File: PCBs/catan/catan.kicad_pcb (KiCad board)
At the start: 2 copper layers, 95.3 x 110 mm, 66 parts, among them J1 Conn_01x04_Female, J2 Conn_01x06_Male, SW1 SW_MEC_5E, SW10 SW_MEC_5E, SW11 SW_MEC_5E, SW2 SW_MEC_5E, SW3 SW_MEC_5E, SW4 SW_MEC_5E, SW5 SW_MEC_5E, SW6 SW_MEC_5E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

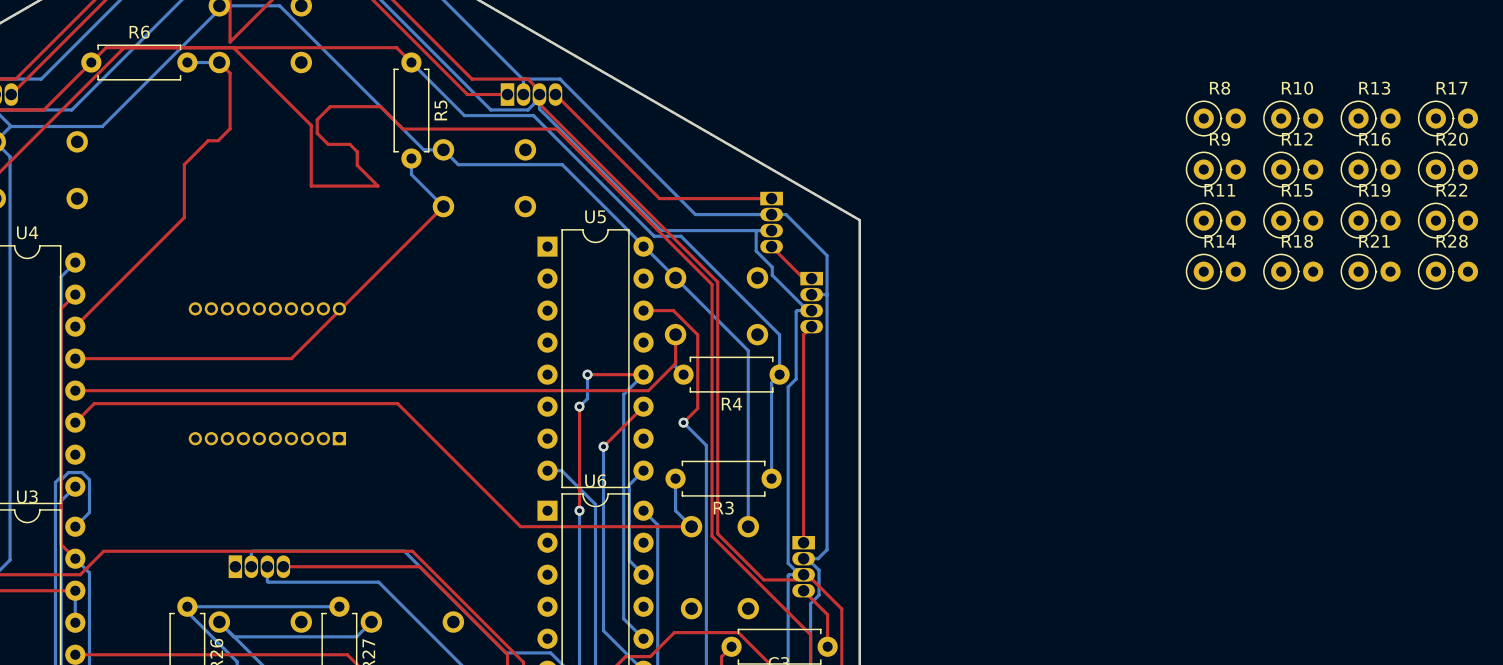
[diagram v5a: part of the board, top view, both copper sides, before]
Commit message: replace segment display
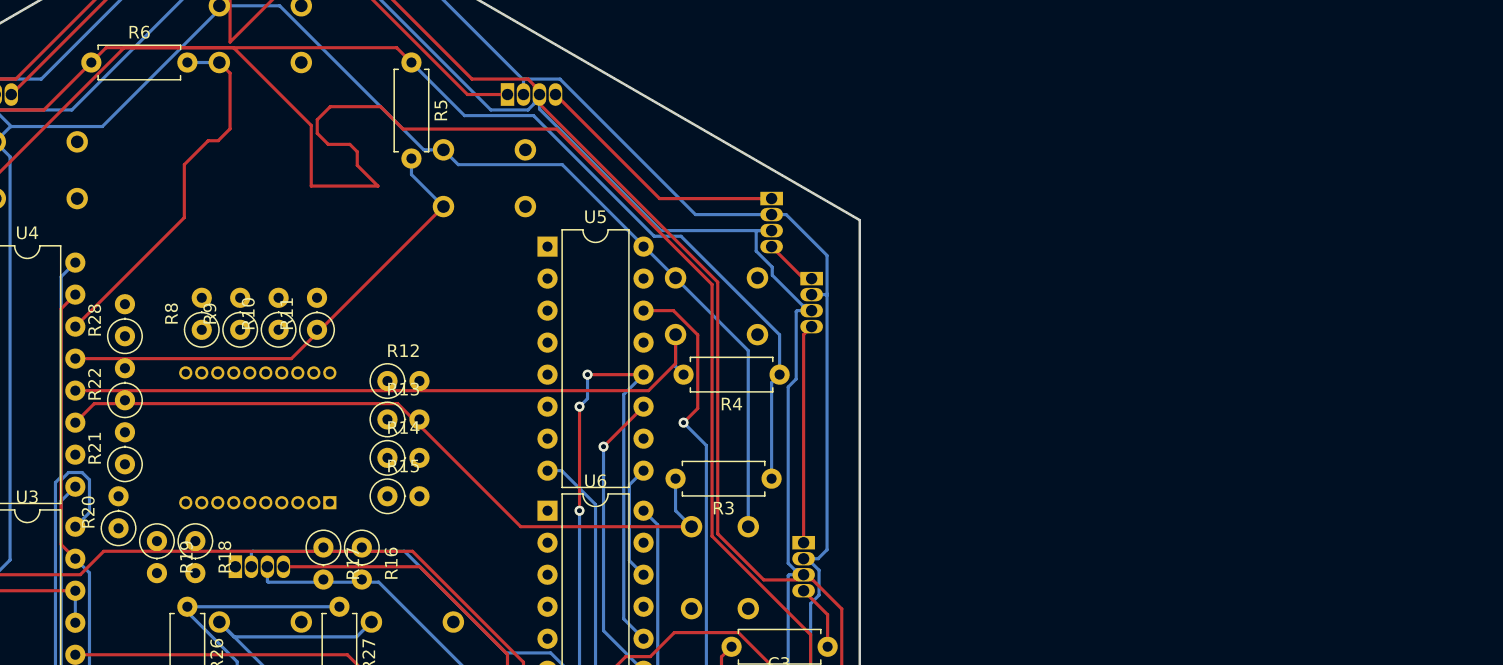
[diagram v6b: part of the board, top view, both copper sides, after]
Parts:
- moved R20 108.3 mm to (113.9, 87.1), turned to 90 degrees
- moved R22 105.0 mm to (114.4, 77.0), turned to 90 degrees
- moved R28 104.1 mm to (114.4, 71.9), turned to 90 degrees
- moved R21 99.1 mm to (114.4, 82.0), turned to 90 degrees
- moved R19 98.7 mm to (117.0, 88.1), turned to 270 degrees
- moved R17 94.6 mm to (130.2, 88.6), turned to 270 degrees
- moved R18 88.8 mm to (120.0, 88.1), turned to 270 degrees
- moved R16 84.6 mm to (133.2, 88.6), turned to 270 degrees
- moved R10 81.3 mm to (126.6, 71.4), turned to 90 degrees
- moved R8 81.3 mm to (120.5, 71.4), turned to 90 degrees
- moved R13 80.7 mm to (135.3, 78.5)
- moved R9 77.5 mm to (123.6, 71.4), turned to 90 degrees
- moved R15 74.2 mm to (135.3, 84.6)
- moved R12 72.9 mm to (135.3, 75.4)
- moved R11 70.9 mm to (129.7, 71.4), turned to 90 degrees
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
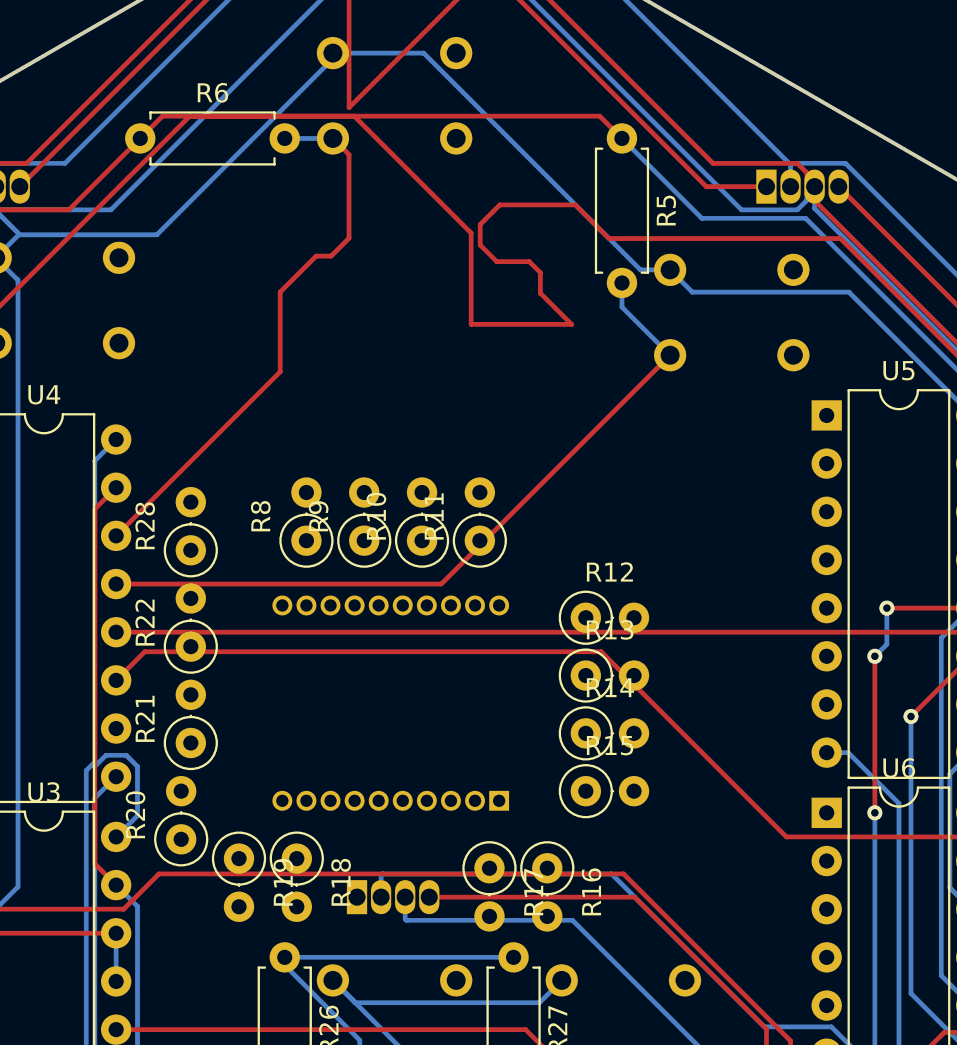
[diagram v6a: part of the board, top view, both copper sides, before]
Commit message: wire display on schematic
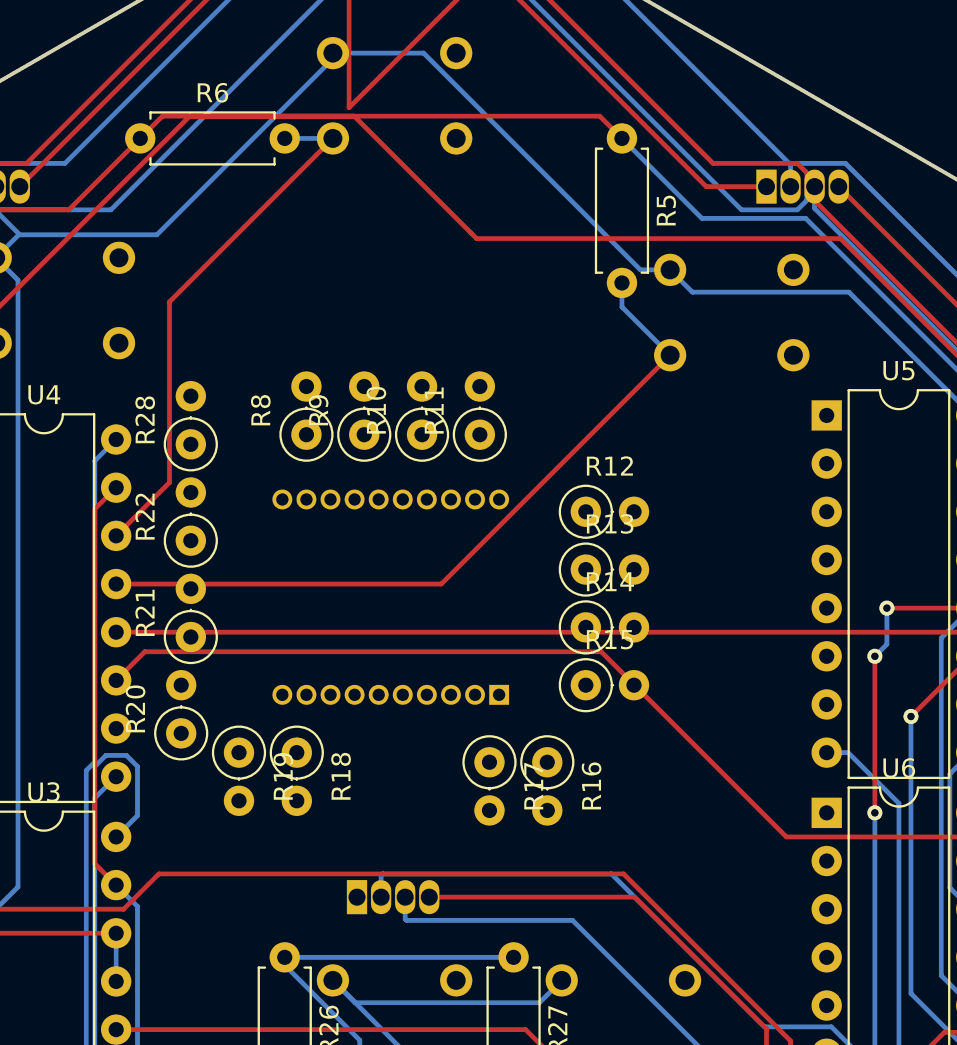
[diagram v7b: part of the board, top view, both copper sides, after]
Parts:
- moved DS1 5.59 mm to (130.7, 79.5)
- moved R12 5.59 mm to (135.3, 69.8)
- moved R13 5.59 mm to (135.3, 72.9)
- moved R14 5.59 mm to (135.3, 75.9)
- moved R18 5.59 mm to (120.0, 82.5)
- moved R19 5.59 mm to (117.0, 82.5)
- moved R21 5.59 mm to (114.4, 76.5)
- moved R22 5.59 mm to (114.4, 71.4)
- moved R28 5.59 mm to (114.4, 66.3)
- moved R10 5.59 mm to (126.6, 65.8)
- moved R11 5.59 mm to (129.7, 65.8)
- moved R15 5.59 mm to (135.3, 79.0)
- moved R16 5.59 mm to (133.2, 83.1)
- moved R17 5.59 mm to (130.2, 83.1)
- moved R20 5.59 mm to (113.9, 81.5)
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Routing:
- net GND: track 996.8 -> 977.9 mm
- net Net-(R6-Pad2): track 29.4 -> 28.2 mm

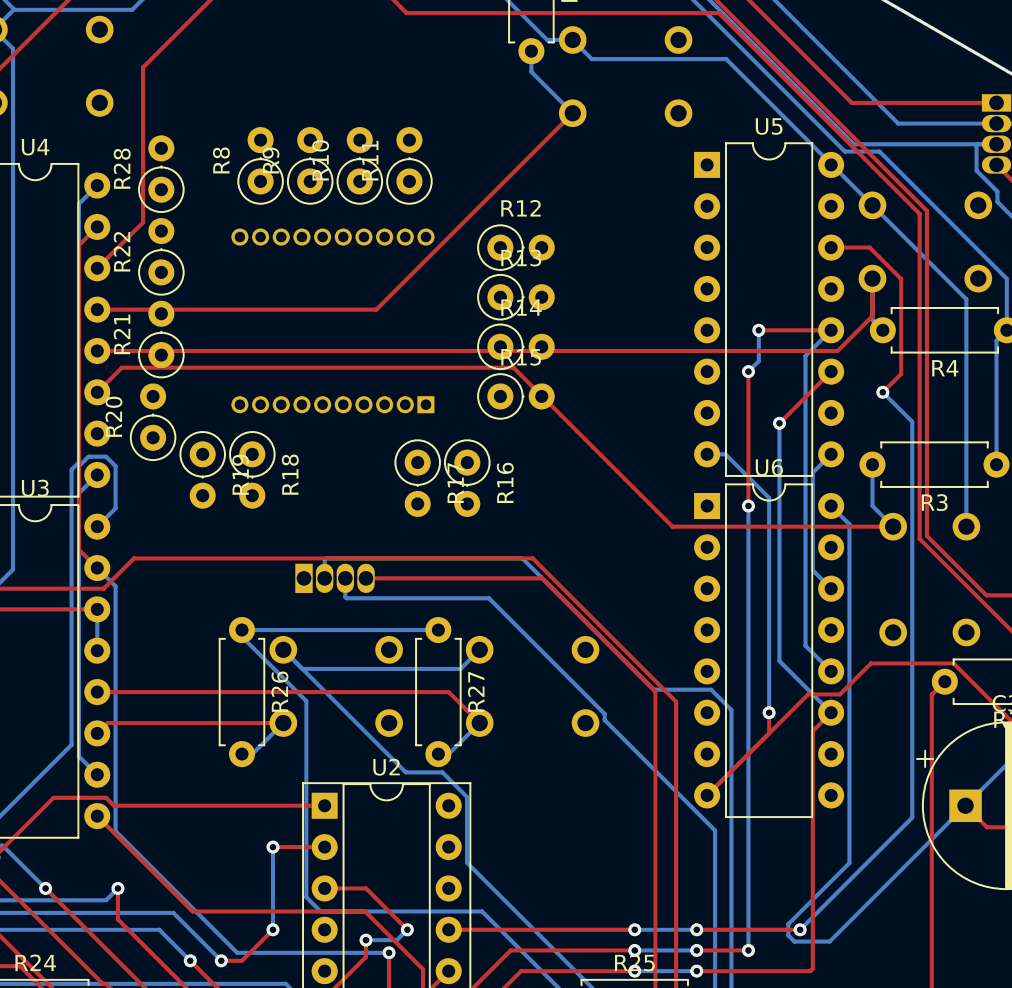
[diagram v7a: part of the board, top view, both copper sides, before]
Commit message: traces for 16 segment
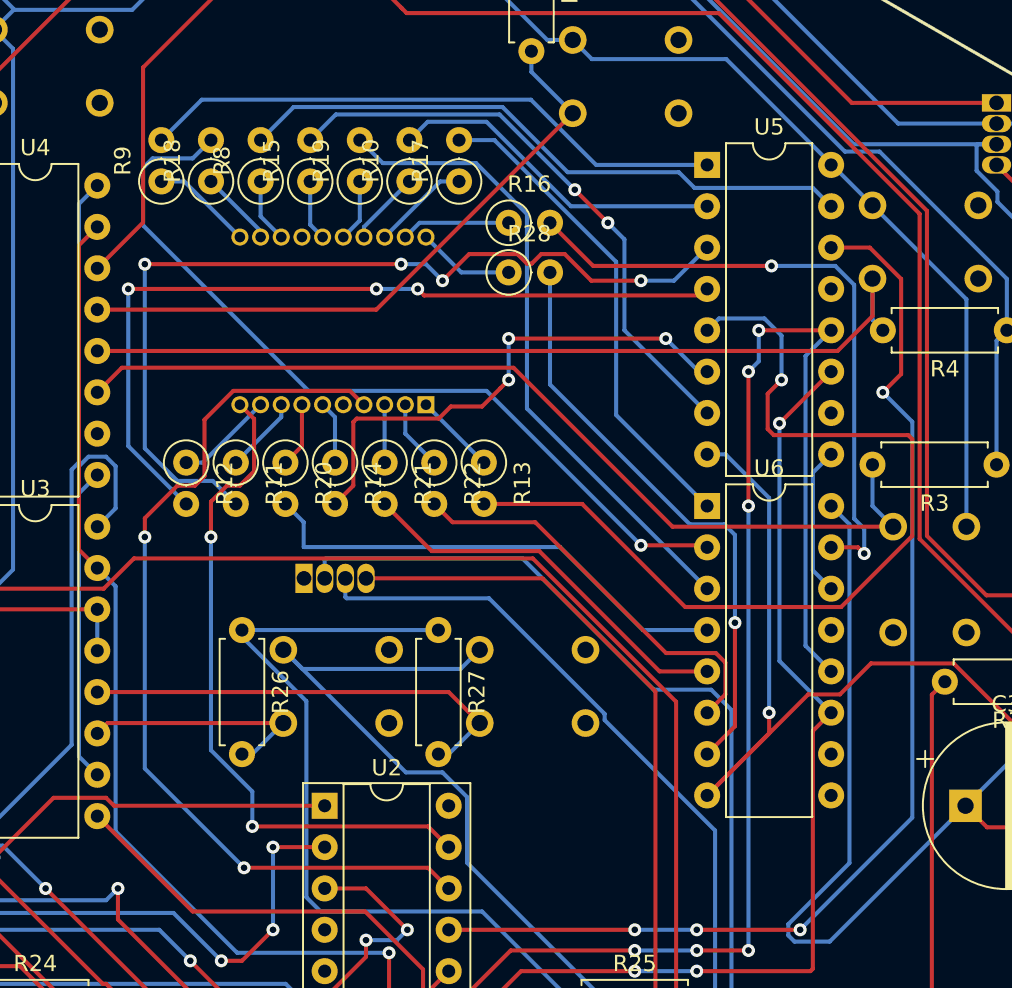
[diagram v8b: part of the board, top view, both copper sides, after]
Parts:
- moved R12 23.4 mm to (116.0, 83.1), turned to 270 degrees
- moved R28 21.9 mm to (135.8, 71.4), turned to 0 degrees
- moved R22 20.4 mm to (131.2, 83.1), turned to 270 degrees
- moved R11 20.3 mm to (119.0, 83.1), turned to 270 degrees
- moved R19 19.3 mm to (126.6, 65.8), turned to 90 degrees
- moved R15 17.6 mm to (123.6, 65.8), turned to 90 degrees
- moved R17 17.5 mm to (132.7, 65.8), turned to 90 degrees
- moved R18 17.0 mm to (117.5, 65.8), turned to 90 degrees
- moved R21 15.2 mm to (128.1, 83.1), turned to 270 degrees
- moved R16 14.9 mm to (135.8, 68.3), turned to 0 degrees
- moved R14 12.4 mm to (125.1, 83.1), turned to 270 degrees
- moved R13 10.2 mm to (134.2, 83.1), turned to 270 degrees
- moved R9 9.14 mm to (114.4, 65.8)
- moved R20 8.27 mm to (122.0, 83.1), turned to 270 degrees
- moved R10 3.05 mm to (129.7, 65.8)
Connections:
- DS1 pad 1: (no net) -> Net-(DS1-Pad1)
- DS1 pad 11: (no net) -> Net-(DS1-Pad11)
- DS1 pad 12: (no net) -> Net-(DS1-Pad12)
- DS1 pad 13: (no net) -> Net-(DS1-Pad13)
- DS1 pad 15: (no net) -> Net-(DS1-Pad15)
- DS1 pad 16: (no net) -> Net-(DS1-Pad16)
- DS1 pad 17: (no net) -> Net-(DS1-Pad17)
- DS1 pad 18: (no net) -> Net-(DS1-Pad18)
- DS1 pad 19: (no net) -> Net-(DS1-Pad19)
- DS1 pad 2: (no net) -> Net-(DS1-Pad2)
- DS1 pad 20: (no net) -> Net-(DS1-Pad20)
- DS1 pad 3: (no net) -> Net-(DS1-Pad3)
- DS1 pad 6: (no net) -> Net-(DS1-Pad6)
- DS1 pad 7: (no net) -> Net-(DS1-Pad7)
- DS1 pad 8: (no net) -> Net-(DS1-Pad8)
- DS1 pad 9: (no net) -> Net-(DS1-Pad9)
- R10 pad 1: (no net) -> Net-(DS1-Pad17)
- R11 pad 1: (no net) -> Net-(DS1-Pad8)
- R12 pad 1: (no net) -> Net-(DS1-Pad9)
- R13 pad 1: (no net) -> Net-(DS1-Pad1)
- R14 pad 1: (no net) -> Net-(DS1-Pad6)
- R15 pad 1: (no net) -> Net-(DS1-Pad15)
- R16 pad 1: (no net) -> Net-(DS1-Pad19)
- R17 pad 1: (no net) -> Net-(DS1-Pad18)
- R18 pad 1: (no net) -> Net-(DS1-Pad12)
- R19 pad 1: (no net) -> Net-(DS1-Pad16)
- R20 pad 1: (no net) -> Net-(DS1-Pad7)
- R21 pad 1: (no net) -> Net-(DS1-Pad3)
- R22 pad 1: (no net) -> Net-(DS1-Pad2)
- R28 pad 1: (no net) -> Net-(DS1-Pad20)
- R8 pad 1: (no net) -> Net-(DS1-Pad13)
- R9 pad 1: (no net) -> Net-(DS1-Pad11)
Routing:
- net Net-(R13-Pad2): track 0.00 -> 57.2 mm, vias 0 -> 1
- net Net-(DS1-Pad4): track 0.00 -> 56.2 mm, vias 0 -> 2
- net Net-(R11-Pad2): track 0.00 -> 56.0 mm, vias 0 -> 4
- net Net-(R18-Pad2): track 0.00 -> 51.3 mm, vias 0 -> 1
- net Net-(R12-Pad2): track 0.00 -> 50.6 mm, vias 0 -> 3
- net Net-(DS1-Pad10): track 0.00 -> 41.5 mm, vias 0 -> 2
- net Net-(R19-Pad2): track 0.00 -> 39.8 mm
- net Net-(R16-Pad2): track 0.00 -> 39.2 mm, vias 0 -> 2
- net Net-(R8-Pad2): track 0.00 -> 38.4 mm
- net Net-(R28-Pad2): track 0.00 -> 36.2 mm, vias 0 -> 1
- net Net-(R9-Pad2): track 0.00 -> 36.2 mm
- net Net-(R15-Pad2): track 0.00 -> 35.9 mm, vias 0 -> 2
- net Net-(R14-Pad2): track 0.00 -> 31.7 mm, vias 0 -> 3
- net Net-(R17-Pad2): track 0.00 -> 30.1 mm
- net Net-(R20-Pad2): track 0.00 -> 30.0 mm
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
